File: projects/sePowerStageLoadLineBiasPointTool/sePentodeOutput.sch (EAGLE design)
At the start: 3 parts

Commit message: updated schematic png
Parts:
- added RC: (no value), holla:R-THRU-H-0.4
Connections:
- new net N$3: RC.1, V2G$1.PK
- net GND: now also RC.2; no longer V2G$1.PK
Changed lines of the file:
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@@
 <part name="S" library="holla" deviceset="SPEAKER-CEM-1201-42" device="" value="4"/>
 <part name="GND1" library="holla" deviceset="GND" device=""/>
+<part name="RC" library="holla" deviceset="R" device="-THRU-H-0.4"/>
 </parts>
 <sheets>
@@
 </instance>
 <instance part="S" gate="G$1" x="81.28" y="50.8" smashed="yes"/>
-<instance part="GND1" gate="1" x="73.66" y="12.7"/>
+<instance part="GND1" gate="1" x="73.66" y="10.16"/>
+<instance part="RC" gate="G$1" x="73.66" y="12.7" rot="R270"/>
 </instances>
 <busses>
@@
 </segment>
 </net>
+<net name="N$3" class="0">
+<segment>
+<pinref part="V2" gate="G$1" pin="PK"/>
+<pinref part="RC" gate="G$1" pin="1"/>
+</segment>
+</net>
 <net name="GND" class="0">
 <segment>
-<pinref part="V2" gate="G$1" pin="PK"/>
+<pinref part="RC" gate="G$1" pin="2"/>
 <pinref part="GND1" gate="1" pin="GND"/>
-<wire x1="73.66" y1="12.7" x2="73.66" y2="15.24" width="0.1524" layer="91"/>
 </segment>
 </net>

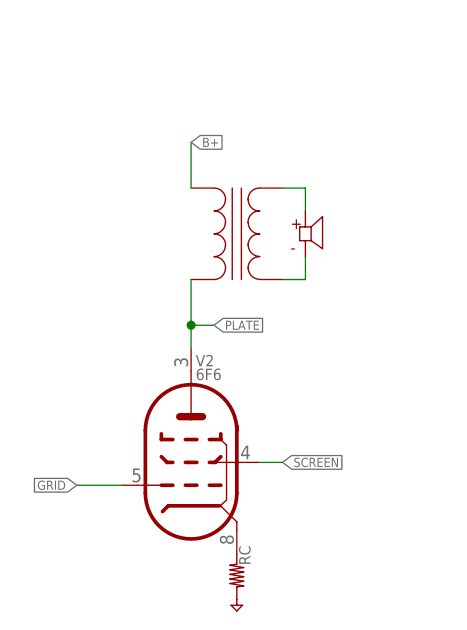
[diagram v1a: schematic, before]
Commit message: added screen resistor and capacitor
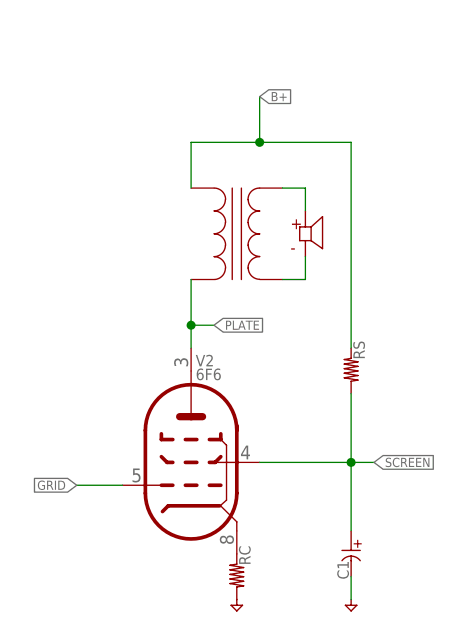
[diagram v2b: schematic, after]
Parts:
- added C1: (no value), holla:C-POLARIZED-E-3
- added RS: (no value), holla:R-THRU-H-0.4
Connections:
- net B+: now also RS.1
- net GND: now also C1.-
- net SCREEN: now also C1.+, RS.2
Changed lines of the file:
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@@
 <part name="GND1" library="holla" deviceset="GND" device=""/>
 <part name="RC" library="holla" deviceset="R" device="-THRU-H-0.4"/>
+<part name="RS" library="holla" deviceset="R" device="-THRU-H-0.4"/>
+<part name="C1" library="holla" deviceset="C-POLARIZED" device="-E-3"/>
+<part name="GND2" library="holla" deviceset="GND" device=""/>
 </parts>
 <sheets>
@@
 <instance part="GND1" gate="1" x="73.66" y="10.16"/>
 <instance part="RC" gate="G$1" x="73.66" y="12.7" rot="R270"/>
+<instance part="RS" gate="G$1" x="86.36" y="35.56" rot="R270"/>
+<instance part="C1" gate="G$1" x="86.36" y="15.24"/>
+<instance part="GND2" gate="1" x="86.36" y="10.16"/>
 </instances>
 <busses>
@@
 <pinref part="T" gate="T1" pin="P1"/>
 <wire x1="68.58" y1="55.88" x2="68.58" y2="60.96" width="0.1524" layer="91"/>
-<label x="68.58" y="60.96" size="1.016" layer="95" xref="yes"/>
+<label x="76.2" y="66.04" size="1.016" layer="95" xref="yes"/>
+<wire x1="68.58" y1="60.96" x2="76.2" y2="60.96" width="0.1524" layer="91"/>
+<pinref part="RS" gate="G$1" pin="1"/>
+<wire x1="76.2" y1="60.96" x2="86.36" y2="60.96" width="0.1524" layer="91"/>
+<wire x1="86.36" y1="60.96" x2="86.36" y2="38.1" width="0.1524" layer="91"/>
+<wire x1="76.2" y1="66.04" x2="76.2" y2="60.96" width="0.1524" layer="91"/>
+<junction x="76.2" y="60.96"/>
 </segment>
 </net>
@@
 <segment>
 <pinref part="V2" gate="G$1" pin="PSG"/>
-<wire x1="76.2" y1="25.4" x2="78.74" y2="25.4" width="0.1524" layer="91"/>
-<label x="78.74" y="25.4" size="1.016" layer="95" xref="yes"/>
+<wire x1="76.2" y1="25.4" x2="86.36" y2="25.4" width="0.1524" layer="91"/>
+<label x="88.9" y="25.4" size="1.016" layer="95" xref="yes"/>
+<pinref part="RS" gate="G$1" pin="2"/>
+<wire x1="86.36" y1="25.4" x2="88.9" y2="25.4" width="0.1524" layer="91"/>
+<wire x1="86.36" y1="33.02" x2="86.36" y2="25.4" width="0.1524" layer="91"/>
+<junction x="86.36" y="25.4"/>
+<pinref part="C1" gate="G$1" pin="+"/>
+<wire x1="86.36" y1="25.4" x2="86.36" y2="17.78" width="0.1524" layer="91"/>
 </segment>
 </net>
@@
 <pinref part="GND1" gate="1" pin="GND"/>
 </segment>
+<segment>
+<pinref part="C1" gate="G$1" pin="-"/>
+<pinref part="GND2" gate="1" pin="GND"/>
+<wire x1="86.36" y1="12.7" x2="86.36" y2="10.16" width="0.1524" layer="91"/>
+</segment>
 </net>

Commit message: changes for video
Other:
- note added: "Rp"
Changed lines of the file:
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@@
 <sheet>
 <plain>
+<text x="68.58" y="50.8" size="1.016" layer="97">Rp</text>
 </plain>
 <instances>

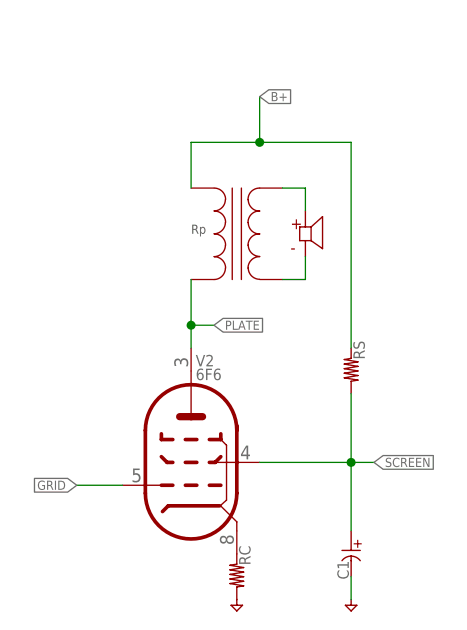
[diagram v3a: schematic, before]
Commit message: added power supply resistance dependence on plate voltage
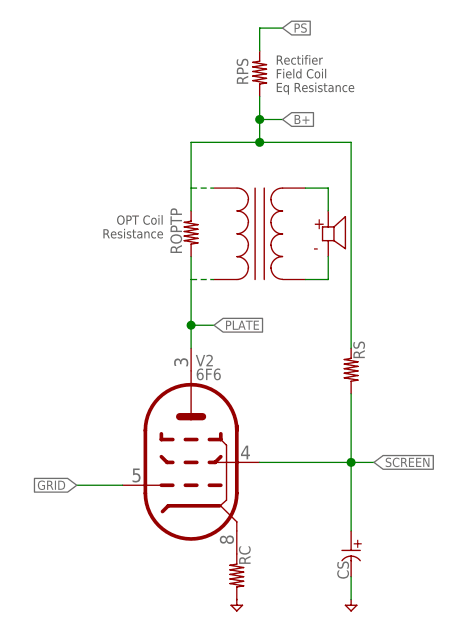
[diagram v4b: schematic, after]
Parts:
- added ROPTP, RPS: (no value), holla:R-THRU-H-0.4
- renumbered C1 to CS
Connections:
- new net PS: RPS.1
- net B+: now also ROPTP.1, RPS.2
- net PLATE: now also ROPTP.2
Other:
- note added: "OPT Coil Resistance"
- note added: "Rectifier Field Coil Eq Resistance"
- note removed: "Rp"
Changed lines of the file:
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@@
 <part name="RC" library="holla" deviceset="R" device="-THRU-H-0.4"/>
 <part name="RS" library="holla" deviceset="R" device="-THRU-H-0.4"/>
-<part name="C1" library="holla" deviceset="C-POLARIZED" device="-E-3"/>
+<part name="CS" library="holla" deviceset="C-POLARIZED" device="-E-3"/>
 <part name="GND2" library="holla" deviceset="GND" device=""/>
+<part name="ROPTP" library="holla" deviceset="R" device="-THRU-H-0.4"/>
+<part name="RPS" library="holla" deviceset="R" device="-THRU-H-0.4"/>
 </parts>
 <sheets>
 <sheet>
 <plain>
-<text x="68.58" y="50.8" size="1.016" layer="97">Rp</text>
+<text x="77.978" y="66.548" size="1.016" layer="97">Rectifier
+Field Coil
+Eq Resistance</text>
+<text x="65.532" y="50.292" size="1.016" layer="97" align="bottom-right">OPT Coil
+Resistance</text>
 </plain>
 <instances>
 <instance part="V2" gate="G$1" x="68.58" y="25.4"/>
-<instance part="T" gate="T1" x="73.66" y="50.8" smashed="yes">
-<attribute name="VALUE" x="73.66" y="42.418" size="1.27" layer="96" align="bottom-center"/>
+<instance part="T" gate="T1" x="76.2" y="50.8" smashed="yes">
+<attribute name="VALUE" x="76.2" y="42.418" size="1.27" layer="96" align="bottom-center"/>
 </instance>
-<instance part="S" gate="G$1" x="81.28" y="50.8" smashed="yes"/>
+<instance part="S" gate="G$1" x="83.82" y="50.8" smashed="yes"/>
 <instance part="GND1" gate="1" x="73.66" y="10.16"/>
 <instance part="RC" gate="G$1" x="73.66" y="12.7" rot="R270"/>
 <instance part="RS" gate="G$1" x="86.36" y="35.56" rot="R270"/>
-<instance part="C1" gate="G$1" x="86.36" y="15.24"/>
+<instance part="CS" gate="G$1" x="86.36" y="15.24"/>
 <instance part="GND2" gate="1" x="86.36" y="10.16"/>
+<instance part="ROPTP" gate="G$1" x="68.58" y="50.8" smashed="yes" rot="R270">
+<attribute name="NAME" x="66.294" y="48.514" size="1.27" layer="95" rot="R270" align="bottom-right"/>
+<attribute name="VALUE" x="68.834" y="49.53" size="1.27" layer="96" rot="R270"/>
+</instance>
+<instance part="RPS" gate="G$1" x="76.2" y="68.58" smashed="yes" rot="R270">
+<attribute name="NAME" x="73.66" y="67.31" size="1.27" layer="95" rot="R270" align="bottom-right"/>
+<attribute name="VALUE" x="76.454" y="67.31" size="1.27" layer="96" rot="R270"/>
+</instance>
 </instances>
 <busses>
@@
 <net name="B+" class="0">
 <segment>
-<pinref part="T" gate="T1" pin="P1"/>
-<wire x1="68.58" y1="55.88" x2="68.58" y2="60.96" width="0.1524" layer="91"/>
-<label x="76.2" y="66.04" size="1.016" layer="95" xref="yes"/>
 <wire x1="68.58" y1="60.96" x2="76.2" y2="60.96" width="0.1524" layer="91"/>
 <pinref part="RS" gate="G$1" pin="1"/>
 <wire x1="76.2" y1="60.96" x2="86.36" y2="60.96" width="0.1524" layer="91"/>
 <wire x1="86.36" y1="60.96" x2="86.36" y2="38.1" width="0.1524" layer="91"/>
-<wire x1="76.2" y1="66.04" x2="76.2" y2="60.96" width="0.1524" layer="91"/>
 <junction x="76.2" y="60.96"/>
+<pinref part="ROPTP" gate="G$1" pin="1"/>
+<wire x1="68.58" y1="60.96" x2="68.58" y2="55.88" width="0.1524" layer="91"/>
+<pinref part="T" gate="T1" pin="P1"/>
+<wire x1="68.58" y1="55.88" x2="68.58" y2="53.34" width="0.1524" layer="91"/>
+<wire x1="68.58" y1="55.88" x2="71.12" y2="55.88" width="0.1524" layer="91" style="shortdash"/>
+<pinref part="RPS" gate="G$1" pin="2"/>
+<wire x1="76.2" y1="66.04" x2="76.2" y2="63.5" width="0.1524" layer="91"/>
+<wire x1="76.2" y1="63.5" x2="76.2" y2="60.96" width="0.1524" layer="91"/>
+<wire x1="76.2" y1="63.5" x2="78.74" y2="63.5" width="0.1524" layer="91"/>
+<label x="78.74" y="63.5" size="1.016" layer="95" xref="yes"/>
+<junction x="76.2" y="63.5"/>
 </segment>
 </net>
@@
 <pinref part="T" gate="T1" pin="S1"/>
 <pinref part="S" gate="G$1" pin="P"/>
-<wire x1="78.74" y1="55.88" x2="81.28" y2="55.88" width="0.1524" layer="91"/>
-<wire x1="81.28" y1="55.88" x2="81.28" y2="53.34" width="0.1524" layer="91"/>
+<wire x1="81.28" y1="55.88" x2="83.82" y2="55.88" width="0.1524" layer="91"/>
+<wire x1="83.82" y1="55.88" x2="83.82" y2="53.34" width="0.1524" layer="91"/>
 </segment>
 </net>
@@
 <pinref part="T" gate="T1" pin="S2"/>
 <pinref part="S" gate="G$1" pin="M"/>
-<wire x1="78.74" y1="45.72" x2="81.28" y2="45.72" width="0.1524" layer="91"/>
-<wire x1="81.28" y1="45.72" x2="81.28" y2="48.26" width="0.1524" layer="91"/>
+<wire x1="81.28" y1="45.72" x2="83.82" y2="45.72" width="0.1524" layer="91"/>
+<wire x1="83.82" y1="45.72" x2="83.82" y2="48.26" width="0.1524" layer="91"/>
 </segment>
 </net>
@@
 <segment>
 <pinref part="V2" gate="G$1" pin="PA"/>
-<pinref part="T" gate="T1" pin="P2"/>
 <wire x1="68.58" y1="38.1" x2="68.58" y2="40.64" width="0.1524" layer="91"/>
-<wire x1="68.58" y1="40.64" x2="68.58" y2="45.72" width="0.1524" layer="91"/>
 <wire x1="68.58" y1="40.64" x2="71.12" y2="40.64" width="0.1524" layer="91"/>
 <label x="71.12" y="40.64" size="1.016" layer="95" xref="yes"/>
 <junction x="68.58" y="40.64"/>
+<pinref part="ROPTP" gate="G$1" pin="2"/>
+<wire x1="68.58" y1="48.26" x2="68.58" y2="45.72" width="0.1524" layer="91"/>
+<pinref part="T" gate="T1" pin="P2"/>
+<wire x1="68.58" y1="45.72" x2="68.58" y2="40.64" width="0.1524" layer="91"/>
+<wire x1="68.58" y1="45.72" x2="71.12" y2="45.72" width="0.1524" layer="91" style="shortdash"/>
 </segment>
 </net>
@@
 <wire x1="86.36" y1="33.02" x2="86.36" y2="25.4" width="0.1524" layer="91"/>
 <junction x="86.36" y="25.4"/>
-<pinref part="C1" gate="G$1" pin="+"/>
+<pinref part="CS" gate="G$1" pin="+"/>
 <wire x1="86.36" y1="25.4" x2="86.36" y2="17.78" width="0.1524" layer="91"/>
 </segment>
@@
 </segment>
 <segment>
-<pinref part="C1" gate="G$1" pin="-"/>
+<pinref part="CS" gate="G$1" pin="-"/>
 <pinref part="GND2" gate="1" pin="GND"/>
 <wire x1="86.36" y1="12.7" x2="86.36" y2="10.16" width="0.1524" layer="91"/>
+</segment>
+</net>
+<net name="PS" class="0">
+<segment>
+<pinref part="RPS" gate="G$1" pin="1"/>
+<wire x1="76.2" y1="71.12" x2="76.2" y2="73.66" width="0.1524" layer="91"/>
+<wire x1="76.2" y1="73.66" x2="78.74" y2="73.66" width="0.1524" layer="91"/>
+<label x="78.74" y="73.66" size="1.016" layer="95" xref="yes"/>
 </segment>
 </net>
@@
 </schematic>
 </drawing>
+<compatibility>
+<note version="6.3" minversion="6.2.2" severity="warning">
+Since Version 6.2.2 text objects can contain more than one line,
+which will not be processed correctly with this version.
+</note>
+</compatibility>
 </eagle>

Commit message: corrected the power supply and output resistance, Vb calculation
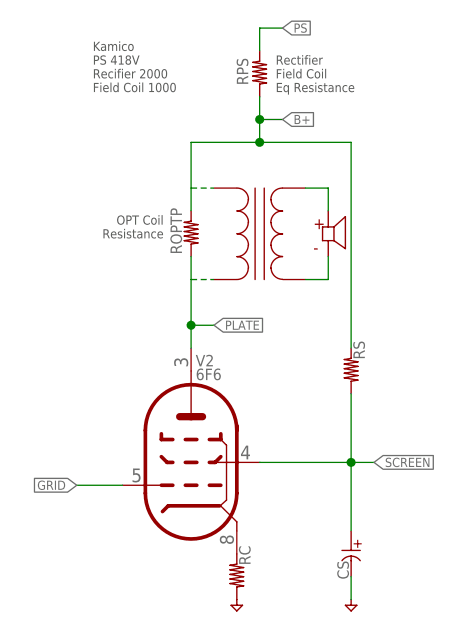
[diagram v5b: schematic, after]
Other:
- note added: "Kamico PS 418V Recifier 2000 Field Coil 1000"
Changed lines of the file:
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@@
 <text x="65.532" y="50.292" size="1.016" layer="97" align="bottom-right">OPT Coil
 Resistance</text>
+<text x="57.658" y="66.548" size="1.016" layer="97">Kamico
+PS 418V
+Recifier 2000
+Field Coil 1000</text>
 </plain>
 <instances>
